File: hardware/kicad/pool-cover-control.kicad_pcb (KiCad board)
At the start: 2 copper layers, 210 x 60 mm, 74 parts, among them J1 Power_Supply _Conn, J2 Motor_Conn, J3 Key_Switch_Conn, J4 Limit_Switch_Conn, J5 SWD_Conn, Q1 DMP4015SK3Q-13, U1 STM32G031K8Tx, U2 ULN2003A, U3 LMR14206, U4 PC817, U5 PC817, U6 PC817, U7 PC817

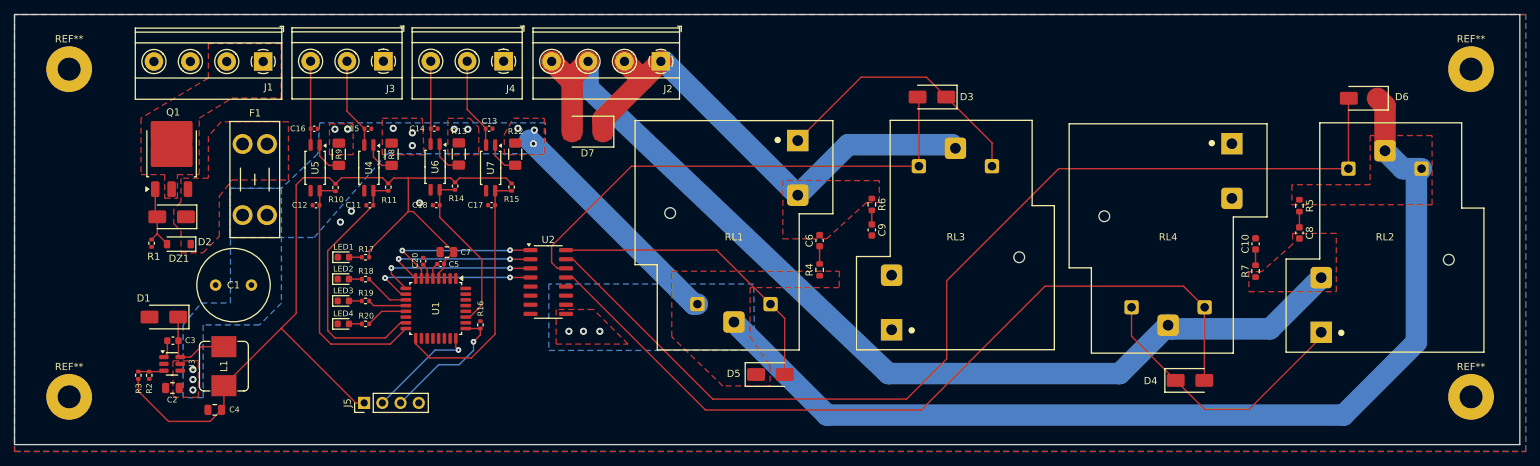
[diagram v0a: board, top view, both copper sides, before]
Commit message: fix(hardware): improve relay sla footprint and add 3d model
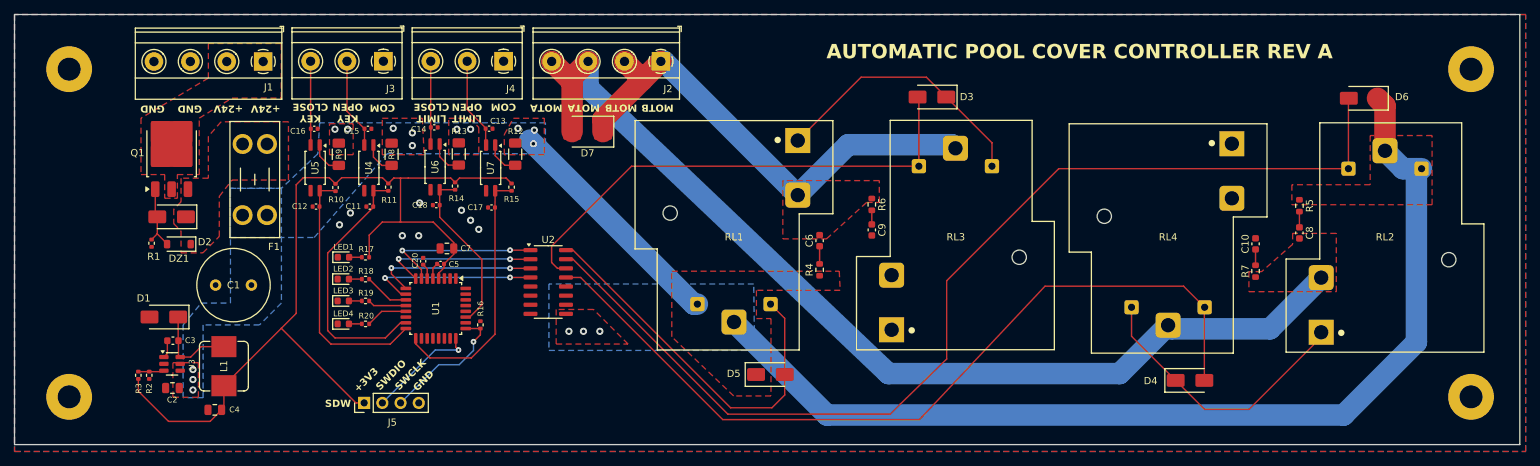
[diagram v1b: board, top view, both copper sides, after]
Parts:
- moved C7 0.51 mm to (106.0, 96.1)
- moved C17 0.33 mm to (112.3, 90.4)
- moved C11 0.19 mm to (95.3, 90.3)
- moved C12 0.19 mm to (87.8, 90.3)
- moved C14 0.18 mm to (104.3, 79.2)
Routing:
- net OUT1: track 42.3 -> 53.9 mm
- net +3V3: track 126.5 -> 128.8 mm
- net OUT2: track 146.8 -> 148.5 mm
- net OUT4: track 115.4 -> 116.8 mm
- net GND: vias 3 -> 8
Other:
- board text added: "+24V"
- board text added: "+3V3"
- board text added: "AUTOMATIC POOL COVER CONTROLLER REV A"
- board text added: "COM"
- board text added: "GND"
- board text added: "Gonzalo G. Fernandez 2026"
- board text added: "KEY CLOSE"
- board text added: "KEY OPEN"
- board text added: "LIMIT CLOSE"
- board text added: "LIMIT OPEN"
- board text added: "MOTA"
- board text added: "MOTB"
- board text added: "SDW"
- board text added: "SWCLK"
- board text added: "SWDIO"

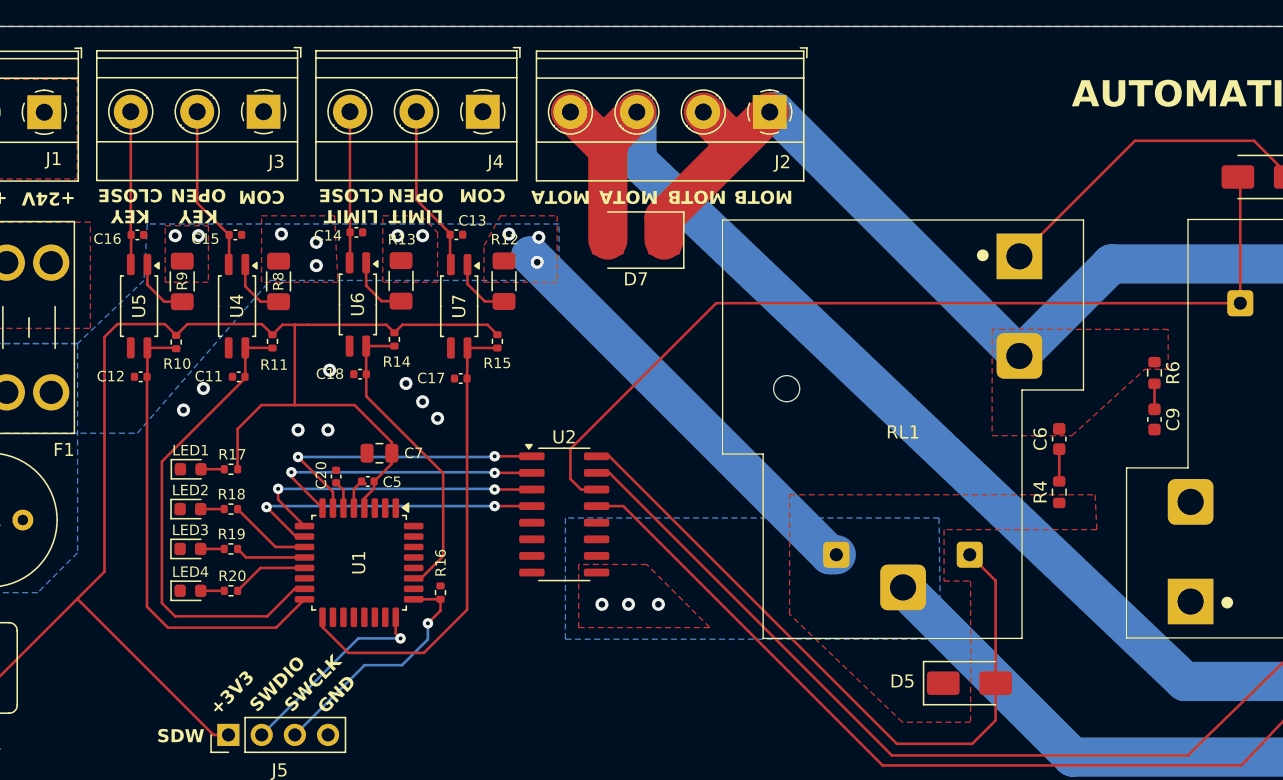
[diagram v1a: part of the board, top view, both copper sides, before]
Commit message: feat(hardware): add 24 vcc pin to limit switch conn for flexibility
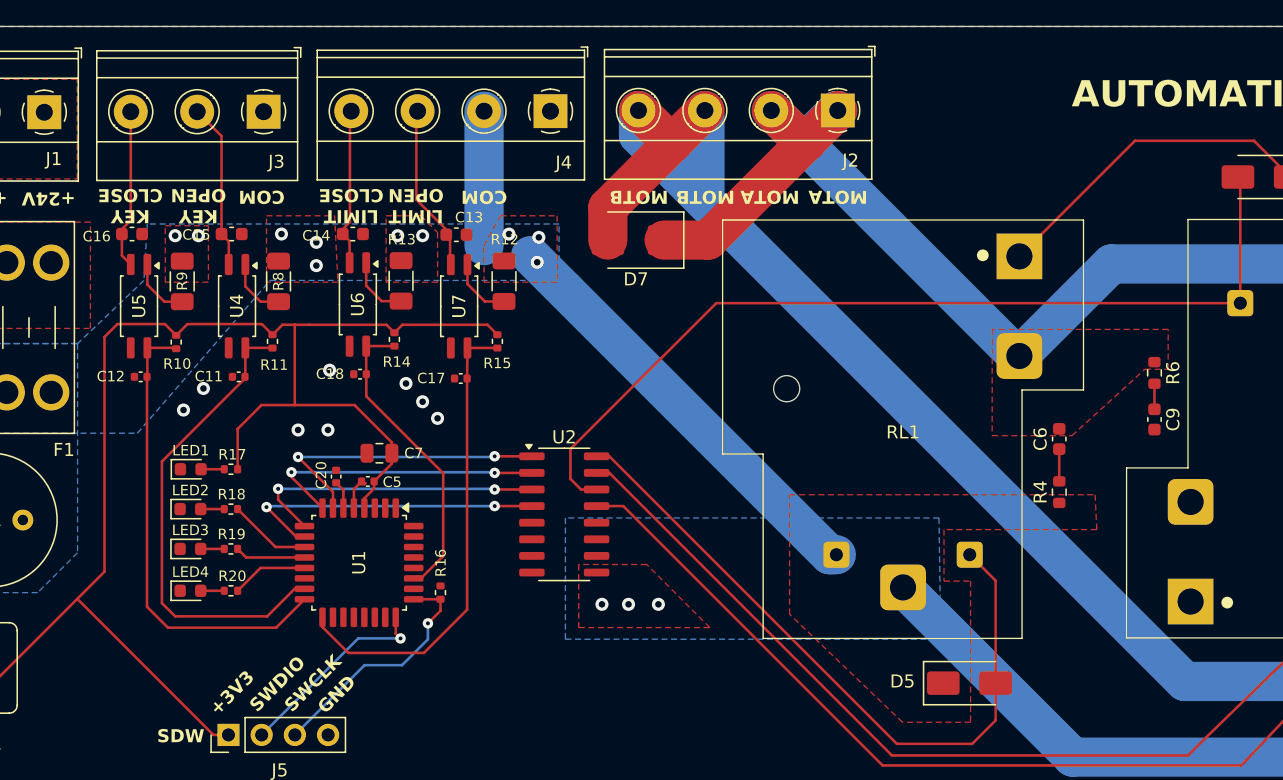
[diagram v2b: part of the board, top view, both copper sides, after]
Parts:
- C13, C14, C15, C16: footprint Capacitor_SMD:C_0402_1005Metric -> Capacitor_SMD:C_0603_1608Metric
- J4: footprint TerminalBlock_Phoenix:TerminalBlock_Phoenix_MKDS-1,5-3-5.08_1x03_P5.08mm_Horizontal -> TerminalBlock_Phoenix:TerminalBlock_Phoenix_MKDS-1,5-4-5.08_1x04_P5.08mm_Horizontal
- moved J2 5.20 mm to (141.1, 69.9)
- moved J4 5.18 mm to (119.1, 70.0)
- moved C16 0.42 mm to (87.1, 79.4)
- moved C14 0.30 mm to (104.0, 79.4)
- moved C15 0.29 mm to (94.7, 79.4)
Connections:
- C13 pad 2: Net-(J4-Pin_2) -> Net-(J4-Pin_3)
- C14 pad 2: Net-(J4-Pin_3) -> Net-(J4-Pin_4)
- J4 pad 2: Net-(J4-Pin_2) -> +24V
- U6 pad 2: Net-(J4-Pin_3) -> Net-(J4-Pin_4)
- U7 pad 2: Net-(J4-Pin_2) -> Net-(J4-Pin_3)
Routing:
- net Net-(J4-Pin_2): track 12.8 -> 0.00 mm
- net Net-(J4-Pin_4): track 0.00 -> 12.1 mm
- net +24V: track 175.8 -> 186.0 mm
- net MOTOR_B: track 142.6 -> 150.9 mm
- net MOTOR_A: track 68.7 -> 76.6 mm
- net Net-(J4-Pin_3): track 11.6 -> 12.8 mm
- net Net-(J3-Pin_3): track 11.7 -> 12.3 mm

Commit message: feat(hardware): add useful testpoints in layout
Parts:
- added REF**: TestPoint_Pad_1.5x1.5mm, TestPoint:TestPoint_Pad_1.5x1.5mm, F.Cu at (67.9, 101.1)
- added REF**: TestPoint_Pad_1.5x1.5mm, TestPoint:TestPoint_Pad_1.5x1.5mm, F.Cu at (97.7, 90.9)
- added REF**: TestPoint_Pad_1.5x1.5mm, TestPoint:TestPoint_Pad_1.5x1.5mm, F.Cu at (115.4, 91.7)
- added REF**: TestPoint_Pad_1.5x1.5mm, TestPoint:TestPoint_Pad_1.5x1.5mm, F.Cu at (78.0, 118.7)
- added REF**: TestPoint_Pad_1.5x1.5mm, TestPoint:TestPoint_Pad_1.5x1.5mm, F.Cu at (109.1, 87.8)
- added REF**: TestPoint_Pad_1.5x1.5mm, TestPoint:TestPoint_Pad_1.5x1.5mm, F.Cu at (61.8, 100.2)
- added REF**: TestPoint_Pad_1.5x1.5mm, TestPoint:TestPoint_Pad_1.5x1.5mm, F.Cu at (93.0, 111.6)
- added REF**: TestPoint_Pad_1.5x1.5mm, TestPoint:TestPoint_Pad_1.5x1.5mm, F.Cu at (82.5, 96.9)
- C11, C12, C17, C18, C20, C5: value 100nF/10V -> 100nF/100V
- C7: value 4.7uF/10V -> 4.7uF/50V
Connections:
- net Net-(D1-K) renamed /LMR14206_SW
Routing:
- net /LMR14206_SW: track 12.4 -> 21.4 mm
- net +24V: track 186.0 -> 192.1 mm
- net KEY_CLOSE: track 35.9 -> 42.0 mm
- net +3V3: track 128.8 -> 133.1 mm
- net LIMIT_OPEN: track 36.3 -> 39.7 mm
- net KEY_OPEN: track 36.5 -> 39.5 mm
- net LIMIT_CLOSE: track 23.6 -> 25.6 mm

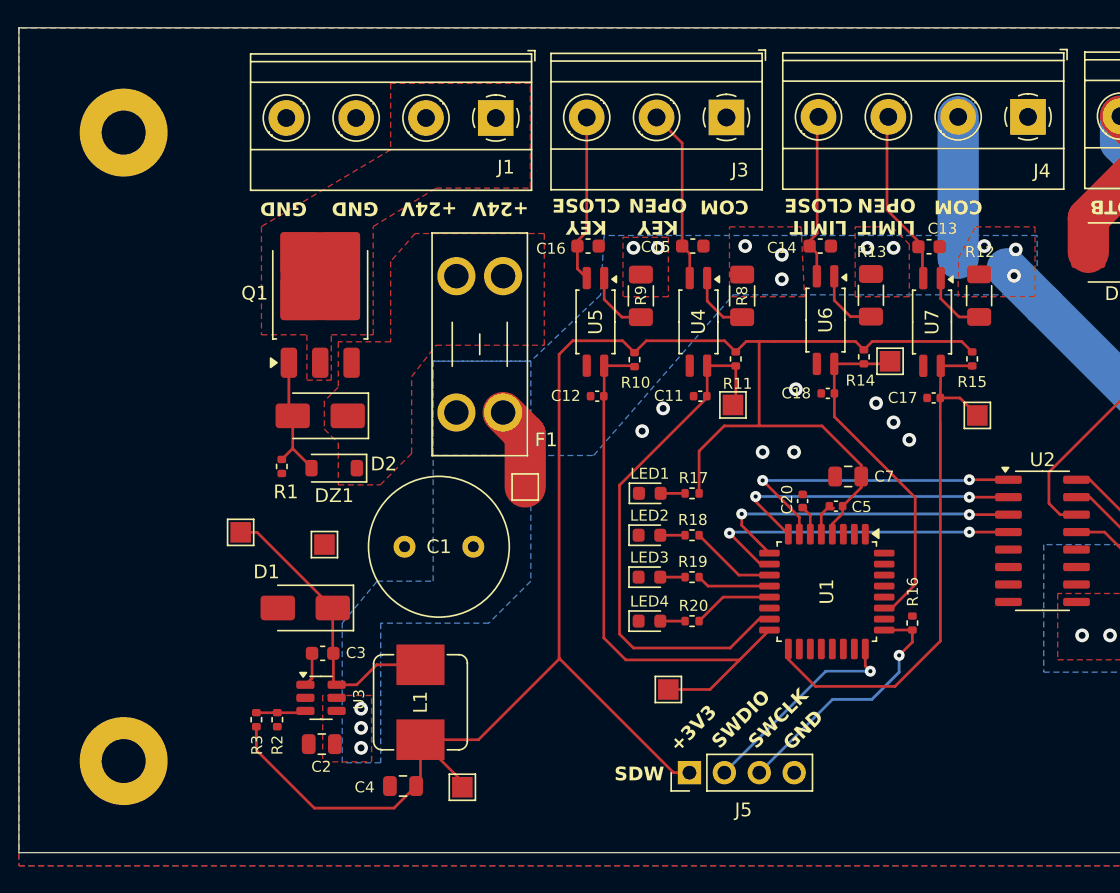
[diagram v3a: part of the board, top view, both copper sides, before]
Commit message: feat(hardware): add custom footprint for fuse holder and optos
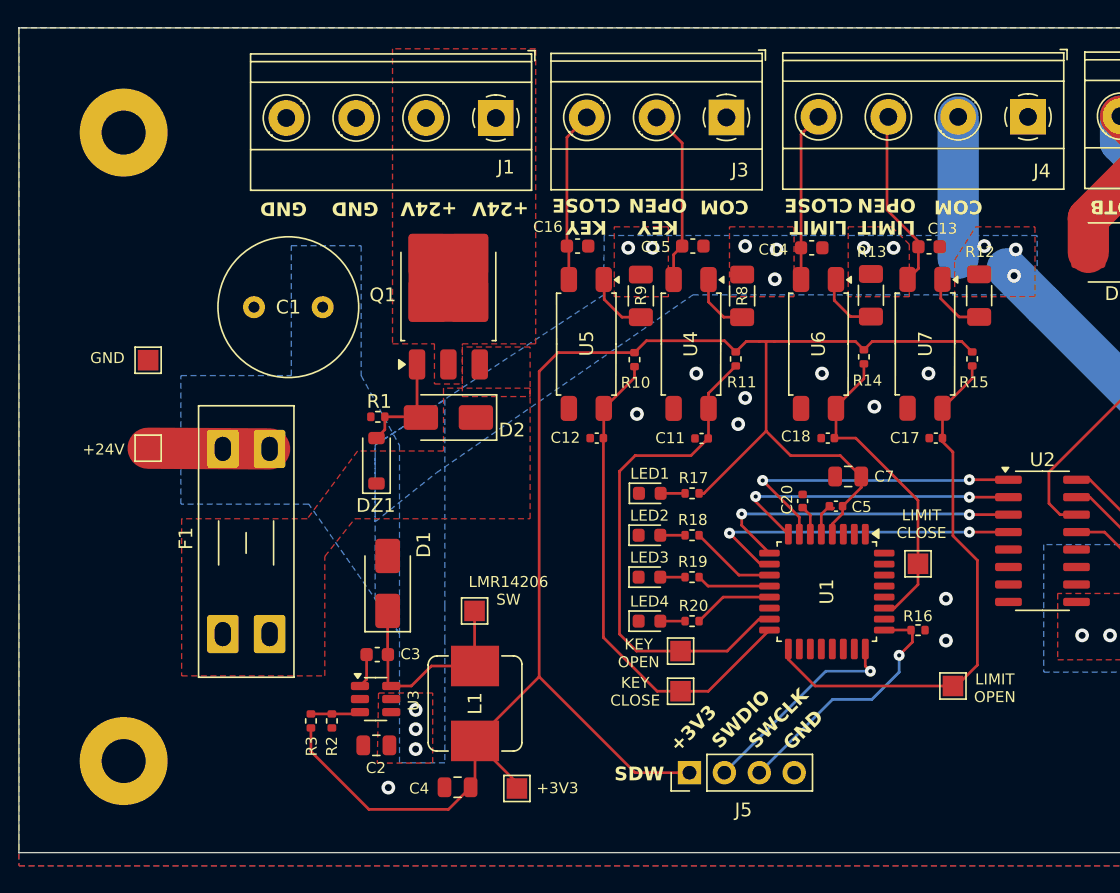
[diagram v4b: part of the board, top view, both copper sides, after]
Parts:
- F1: footprint Fuse:Fuseholder_Blade_Mini_Keystone_3568 -> pool-cover-control:Fuseholder_Blade_Mini_XFCN XF-508P-A-B
- U4, U5, U6, U7: footprint Package_SO:SOP-4_4.4x2.6mm_P1.27mm -> pool-cover-control:SOP-4_7.5x4.1mm_P2.54mm
- moved F1 33.1 mm to (60.6, 107.6), turned to 90 degrees
- moved REF** 27.6 mm to (55.1, 94.1)
- moved C1 20.6 mm to (67.8, 83.8)
- moved REF** 19.8 mm to (113.7, 111.4)
- moved REF** 18.6 mm to (55.1, 87.7)
- moved REF** 18.3 mm to (93.9, 108.8)
- moved REF** 18.0 mm to (78.9, 105.9)
- moved REF** 14.9 mm to (111.1, 102.5)
- moved D2 9.32 mm to (77.0, 91.8)
- moved Q1 9.32 mm to (77.0, 82.9)
- moved R1 7.87 mm to (71.8, 91.8), turned to 180 degrees
- moved D1 6.25 mm to (72.5, 103.9), turned to 90 degrees
- moved C2 3.97 mm to (71.7, 115.7)
- moved C3 3.97 mm to (71.8, 109.1)
- moved C4 3.97 mm to (77.6, 118.7)
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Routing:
- net +3V3: track 133.1 -> 127.2 mm
- net KEY_CLOSE: track 42.0 -> 36.3 mm
- net /LMR14206_SW: track 21.4 -> 16.4 mm
- net +24V: track 192.1 -> 194.9 mm
- net LIMIT_CLOSE: track 25.6 -> 23.5 mm
- net KEY_OPEN: track 39.5 -> 37.8 mm
- net Net-(D2-A): track 9.48 -> 8.92 mm
- net GND: vias 8 -> 10
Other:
- board text added: "LMR14206 SW"

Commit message: fix(hardware): review for JLCPCB standard parts
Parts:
- C10, C6, C8, C9: value 10nF/100V -> 10nF/50V
- C11, C12, C17, C18, C20, C5: value 100nF/100V -> 100nF/16V
- C2: footprint Capacitor_SMD:C_0805_2012Metric -> Capacitor_SMD:C_1206_3216Metric
- C3: value 0.15uF -> 220nF
- C4: value 47uF/10V -> 22uF/25V; footprint Capacitor_SMD:C_0805_2012Metric -> Capacitor_SMD:C_1206_3216Metric
- C7: value 4.7uF/50V -> 4.7uF/25V
- R16: footprint Resistor_SMD:R_0402_1005Metric -> Resistor_SMD:R_0603_1608Metric
- R18: value 100 -> 330
- R2: value 1.02k -> 3k; footprint Resistor_SMD:R_0402_1005Metric -> Resistor_SMD:R_0603_1608Metric
- R3: value 3.4k -> 10k; footprint Resistor_SMD:R_0402_1005Metric -> Resistor_SMD:R_0603_1608Metric
- moved R3 0.71 mm to (66.3, 114.2)
- moved R16 0.42 mm to (111.5, 107.3)
- moved R2 0.32 mm to (68.3, 114.2)
- moved C2 0.30 mm to (71.8, 116.0)
- moved C4 0.19 mm to (77.4, 118.8)
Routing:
- net +3V3: track 127.2 -> 129.1 mm
- net Net-(U3-FB): track 3.62 -> 4.44 mm
- net +24V: vias 16 -> 15
